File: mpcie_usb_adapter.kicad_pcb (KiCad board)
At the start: 2 copper layers, 85 x 56 mm, 15 parts, among them J1 USB4105-GF-A, J2 SMA-J-P-H-ST-EM1, J3 SMA-J-P-H-ST-EM1, J4 Conn_Coaxial_Small, J5 Conn_Coaxial_Small, U1 LD1117S33TR, U2 AS-RTK2B-MPCIE-L1L2-F9P-01

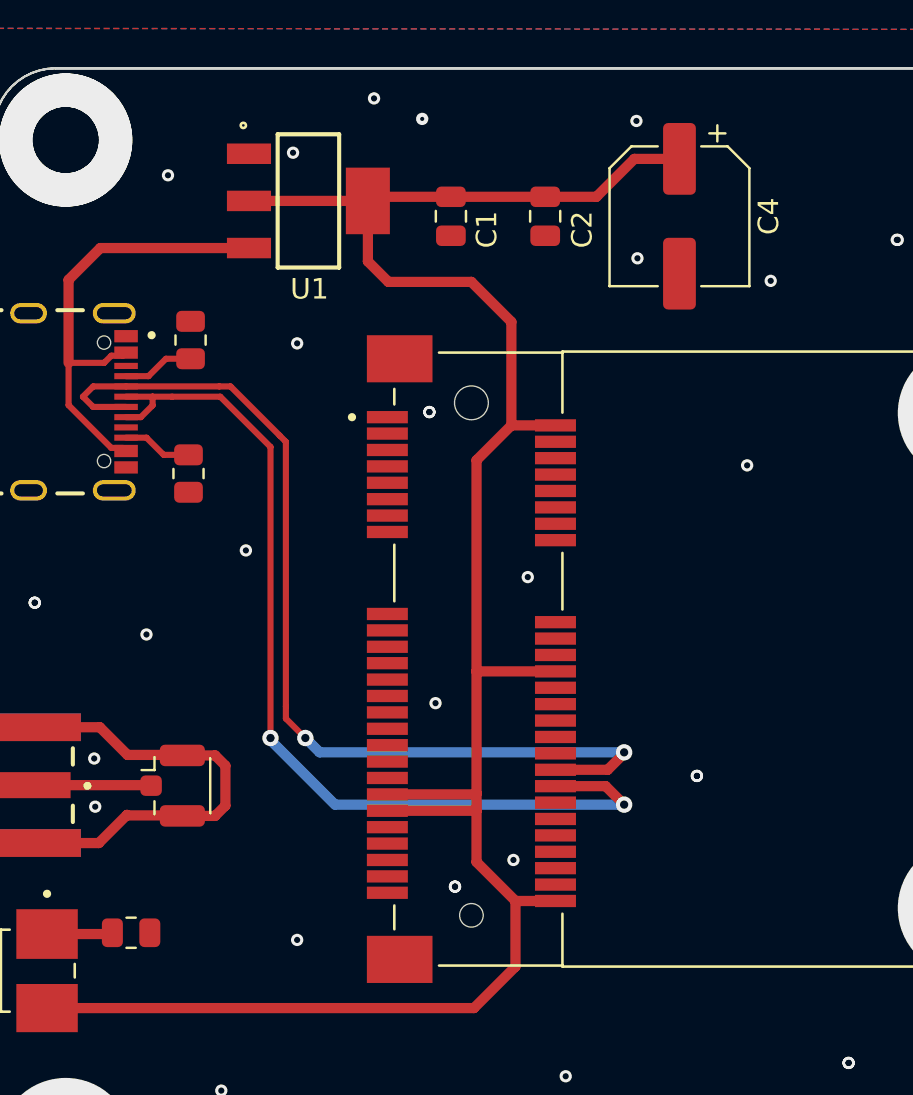
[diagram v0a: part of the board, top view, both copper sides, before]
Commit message: added ESD protection diodes and capacitors
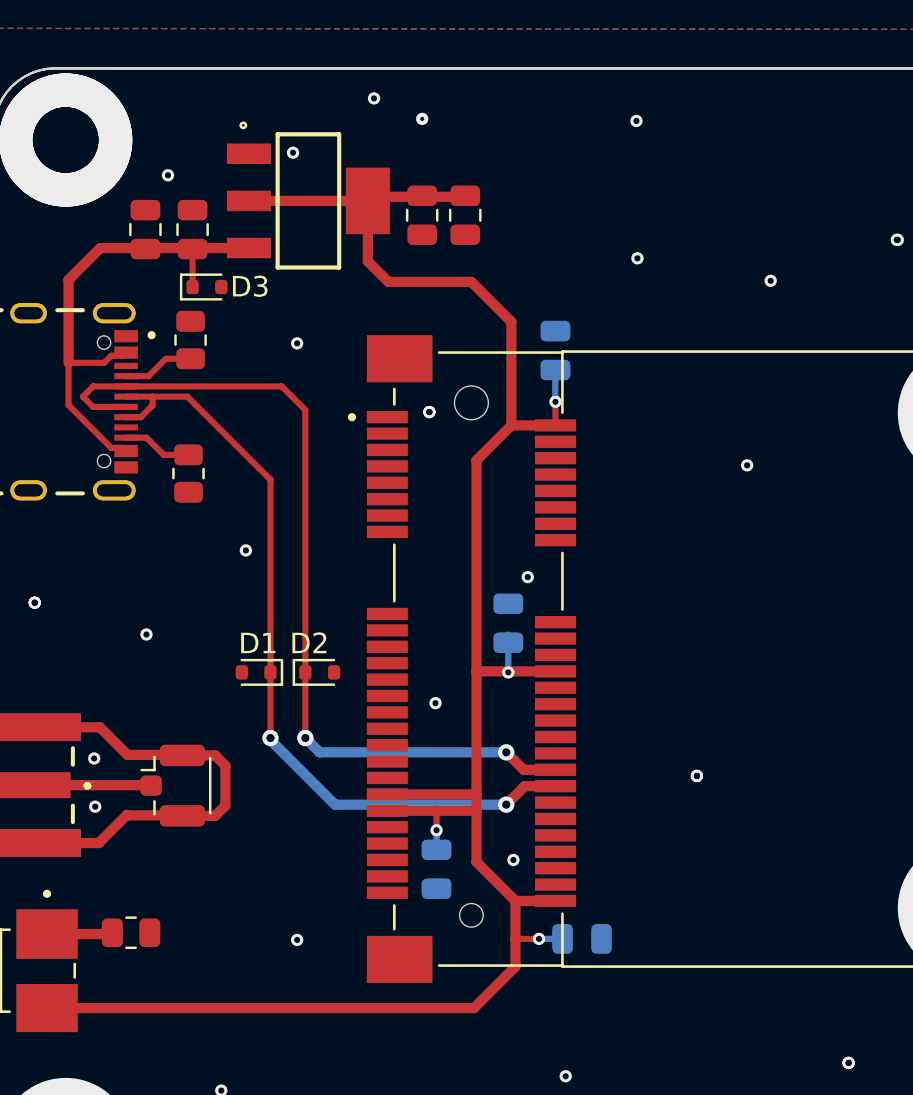
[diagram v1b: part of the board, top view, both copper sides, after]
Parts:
- added C3: 100nF, Capacitor_SMD:C_0805_2012Metric, F.Cu at (176.8, 73.1)
- added C5: 100nF, Capacitor_SMD:C_0805_2012Metric, B.Cu at (196.8, 79.0)
- added C6: 100nF, Capacitor_SMD:C_0805_2012Metric, B.Cu at (194.5, 92.3)
- added C7: 100nF, Capacitor_SMD:C_0805_2012Metric, B.Cu at (198.1, 107.7)
- added C8: 100nF, Capacitor_SMD:C_0805_2012Metric, B.Cu at (191.0, 104.3)
- added D1: ESD321, Diode_SMD:D_SOD-523, F.Cu at (182.2, 94.7)
- added D2: ESD321, Diode_SMD:D_SOD-523, F.Cu at (185.3, 94.7)
- added D3: ESD441, Diode_SMD:D_SOD-523, F.Cu at (179.8, 75.9)
- C1: value 10nF -> 100nF
- C2: value 100nF -> 10uF
- C4: value 100uF -> 10uF; footprint Capacitor_SMD:CP_Elec_6.3x5.4 -> Capacitor_SMD:C_0805_2012Metric
- moved C4 23.8 mm to (179.1, 73.1), turned to 90 degrees
- moved C2 3.90 mm to (192.4, 72.4)
- moved C1 1.40 mm to (190.3, 72.4)
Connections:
- C4 pad 1: +3.3V -> +5V
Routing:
- net USB_D+: track 46.7 -> 39.1 mm
- net USB_D-: track 48.1 -> 42.8 mm
- net +3.3V: track 105.6 -> 103.2 mm, vias 0 -> 4
- net +5V: track 22.6 -> 24.5 mm
- net GND: vias 54 -> 52

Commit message: reworked pcb
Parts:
- C5, C6, C7, C8: moved to F.Cu
- moved D2 15.2 mm to (180.2, 80.4), turned to 90 degrees
- moved C3 13.2 mm to (189.7, 70.2)
- moved D1 11.7 mm to (180.2, 83.2), turned to -90 degrees
- moved C4 8.90 mm to (186.6, 68.3), turned to 0 degrees
- moved C8 6.67 mm to (185.7, 100.2), turned to 90 degrees
- moved C5 5.51 mm to (199.5, 83.8), turned to -90 degrees
- moved C6 5.17 mm to (199.5, 93.6)
- moved C7 3.36 mm to (199.5, 104.7), turned to 90 degrees
- moved D3 3.21 mm to (176.7, 75.3), turned to 180 degrees
- moved C1 2.96 mm to (189.7, 75.3)
- moved C2 2.96 mm to (191.8, 75.3)
- moved U1 1.86 mm to (184.0, 73.4), turned to 180 degrees
- moved R5 0.95 mm to (175.2, 107.7), turned to 90 degrees
- moved R1 0.69 mm to (179.2, 85.6), turned to 0 degrees
- moved R2 0.59 mm to (179.2, 78.0), turned to 0 degrees
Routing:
- net +3.3V: track 103.2 -> 22.0 mm, vias 4 -> 0
- net Net-(J4-Ext): track 21.4 -> 0.00 mm
- net Net-(J5-Ext): track 20.5 -> 0.00 mm
- net +5V: track 24.5 -> 35.3 mm, vias 0 -> 10
- net USB_D-: track 42.8 -> 38.3 mm, vias 2 -> 0
- net USB_D+: track 39.1 -> 37.4 mm, vias 2 -> 0
- net GND: track 0.00 -> 1.11 mm, vias 52 -> 176
- net Net-(J1-CC2): track 3.39 -> 4.34 mm
- added copper zone on F.Cu, net +3.3V
- added copper zone on F.Cu, net +5V
- added copper zone on F.Cu, net Net-(J4-Ext)
- added copper zone on F.Cu, net Net-(J5-Ext)
